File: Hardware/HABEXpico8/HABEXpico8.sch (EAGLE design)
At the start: 28 parts, among them Q1 2.5A/30V, U1 LTC3106, U2 EVA-8M, U3 STM32L011G4, Y1 ABS07-120-32.768KHZ-T

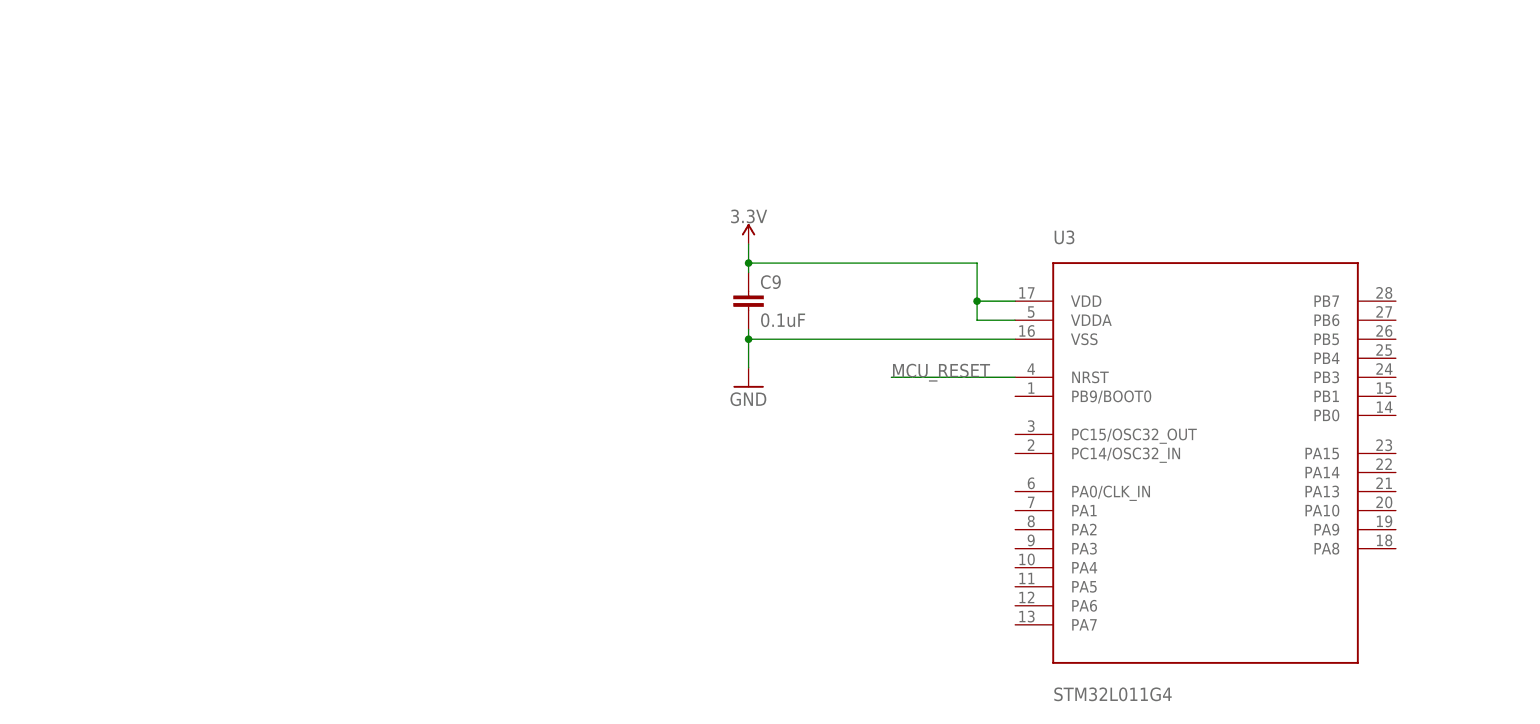
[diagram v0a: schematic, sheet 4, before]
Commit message: Updated schematic design
Power save support ICs, updated power budget
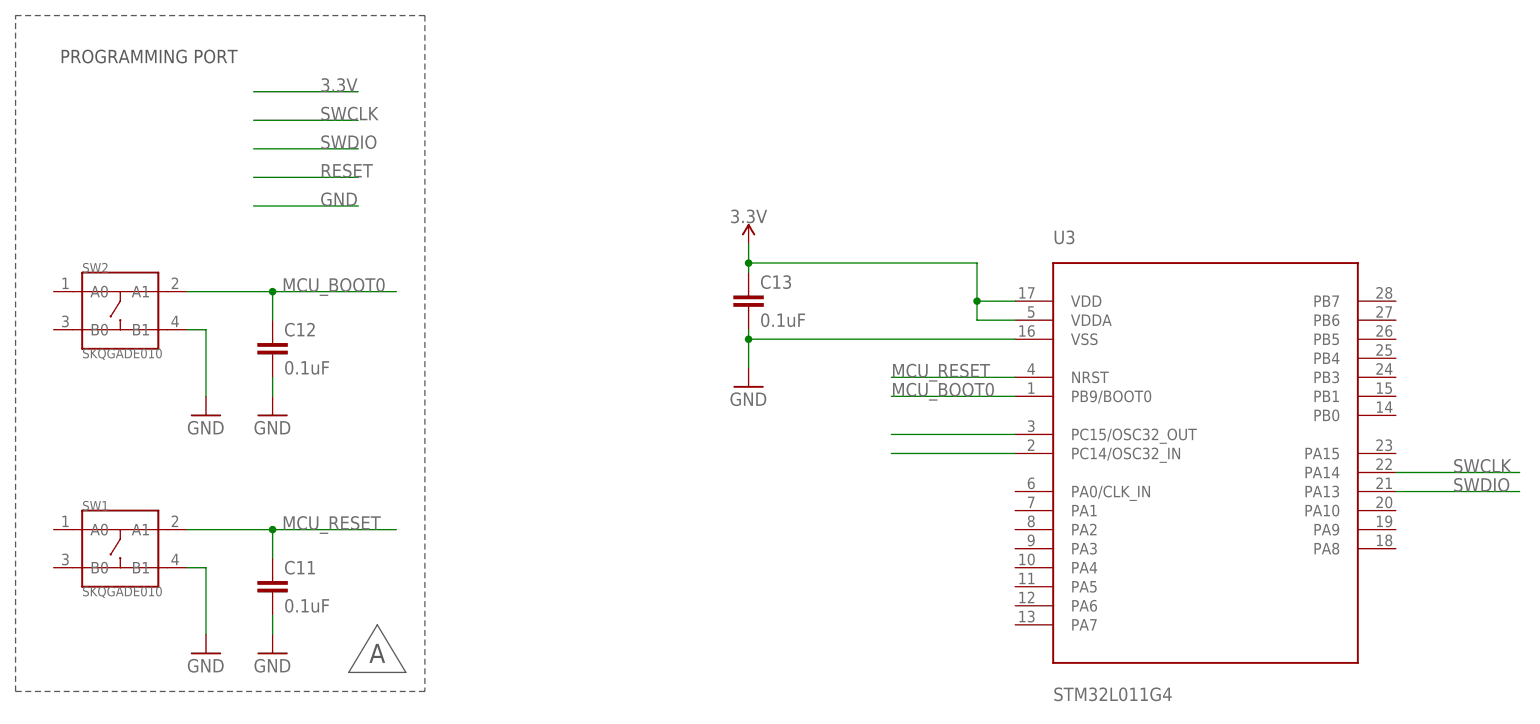
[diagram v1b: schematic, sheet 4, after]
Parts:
- added C12, C13: 0.1uF, SparkFun-Capacitors:0.1UF-0603-25V-5%
- added SW1, SW2: SKQGADE010, Seeed-Switch:SMD-BUTTON(4P-5.2X5.2X1.5MM-SKQGADE010)-SKQGADE010
- C11: value 6pF -> 0.1uF; device rcl:C-EUC0603 -> SparkFun-Capacitors:0.1UF-0603-25V-5%
- C9: value 0.1uF -> 6pF; device SparkFun-Capacitors:0.1UF-0603-25V-5% -> rcl:C-EUC0603
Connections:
- new net MCU_BOOT0: C12.1, SW2.A1, U3.PB9/BOOT0
- new net N$8: U3.PC15/OSC32_OUT
- new net N$9: U3.PC14/OSC32_IN
- new net SWCLK: U3.PA14
- new net SWDIO: U3.PA13
- net 3.3V: now also C13.1; no longer C9.1
- net GND: now also C12.2, C13.2, SW1.B1, SW2.B1
- net MCU_RESET: now also C11.1, SW1.A1
- net N$6: now also C9.1; no longer C10.1
- net N$7: now also C10.1; no longer C11.1
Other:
- note added: "3. RTC ENABLES POWER SAVE MODE, ALLOWS FOR GPS TRACKING USING ONLY SOLAR POWER 2. CRYSTAL 32.7680KHZ 6PF SMD, 3.20MM x 1.5MM 1. ENHANCEMENT-MODE P-CHANNEL MOSFET NOTES: THIS PAGE"
- note added: "A"
- note added: "PROGRAMMING PORT"
- note added: "SUPPORT HARDWARE, NOT FOR FLIGHT 1. BOARD DESIGN FOR PROGRAMMING, TESTING, AND QUALIFYING DEVICES NOTES: THIS PAGE"
- note removed: "1. BOARD DESIGN IS FOR TEST, DEBUG, QUALIFICATION, AND GSE PURPOSES NOTES: THIS PAGE"
- note removed: "3. RTC ENABLES POWER SAVE MODE, ALLOWS FOR GPS TRACKING ON SOLAR POWER ONLY 2. CRYSTAL 32.7680KHZ 6PF SMD, 3.20MM x 1.5MM 1. ENHANCEMENT-MODE P-CHANNEL MOSFET NOTES: THIS PAGE"
- moved on the sheet: C10
